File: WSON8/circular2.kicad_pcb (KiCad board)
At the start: 2 copper layers, 25 x 25 mm, 34 parts, among them J101 Conn_Coaxial, J102 Conn_01x03, U101 LT3042xMSE, U102 LT3093xMSE, U103 OPA859xDSG

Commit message: add ohwr-texts to wson8 files
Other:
- board text added: "Copyright Anders E E Wallin, 2020. This documentation describes Open Hardware and is licensed under the CERN OHL v. 1.2. You may redistribute and modify this documentation under the terms of the CERN OHL v.1.2. (http://ohwr.org/cernohl). This documentation is distributed WITHOUT ANY EXPRESS OR IMPLIED WARRANTY, INCLUDING OF MERCHANTABILITY, SATISFACTORY QUALITY AND FITNESS FOR A PARTICULAR PURPOS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"
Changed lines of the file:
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@@
   (general
     (thickness 1.6)
-    (drawings 23)
+    (drawings 28)
     (tracks 282)
     (zones 0)
@@
   )
   (page A4)
+  (title_block
+    (title "One Inch Photodetector - WSON8")
+    (date 2020-02)
+    (company "anders.e.e.wallin \"at\" gmail.com")
+  )
   (layers
     (0 F.Cu signal)
@@
     )
   )
+  (gr_line (start 210 40) (end 210 20) (layer Dwgs.User) (width 0.15))
+  (gr_line (start 280 40) (end 210 40) (layer Dwgs.User) (width 0.15))
+  (gr_line (start 280 20) (end 280 40) (layer Dwgs.User) (width 0.15))
+  (gr_line (start 210 20) (end 280 20) (layer Dwgs.User) (width 0.15))
+  (gr_text "Copyright Anders E E Wallin, 2020.\nThis documentation describes Open Hardware and is licensed under the\nCERN OHL v. 1.2.\nYou may redistribute and modify this documentation under the terms of the\nCERN OHL v.1.2. (http://ohwr.org/cernohl). This documentation is distributed\nWITHOUT ANY EXPRESS OR IMPLIED WARRANTY, INCLUDING OF\nMERCHANTABILITY, SATISFACTORY QUALITY AND FITNESS FOR A\nPARTICULAR PURPOSE. Please see the CERN OHL v.1.2 for applicable\nconditions\n" (at 216 30) (layer Dwgs.User)
+    (effects (font (size 1 1) (thickness 0.15)) (justify left))
+  )
   (gr_text - (at 160.25 101) (layer F.SilkS)

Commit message: save wson
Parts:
- C102, C110, C111: value C -> 4u7
- C104: value C -> 10n
- C108, C109: value C -> 100n
- R101, R107: value 49k9 -> 25k
- R103: value R -> 0R
- R106: value R -> 49R9
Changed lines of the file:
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@@
-(kicad_pcb (version 20171130) (host pcbnew 5.1.5-52549c5~84~ubuntu18.04.1)
+(kicad_pcb (version 20171130) (host pcbnew 5.1.5-52549c5~86~ubuntu18.04.1)
   (general
     (thickness 1.6)
@@
       (effects (font (size 0.5 0.5) (thickness 0.1)))
     )
-    (fp_text value 49k9 (at 0 1.43) (layer F.Fab)
+    (fp_text value 25k (at 0 1.43) (layer F.Fab)
       (effects (font (size 1 1) (thickness 0.15)))
     )
@@
       (effects (font (size 0.5 0.5) (thickness 0.1)))
     )
-    (fp_text value R (at 0 1.43 45) (layer F.Fab)
+    (fp_text value 49R9 (at 0 1.43 45) (layer F.Fab)
       (effects (font (size 1 1) (thickness 0.15)))
     )
@@
       (effects (font (size 0.5 0.5) (thickness 0.1)) (justify mirror))
     )
-    (fp_text value R (at 0 -1.43 90) (layer B.Fab)
+    (fp_text value 0R (at 0 -1.43 90) (layer B.Fab)
       (effects (font (size 1 1) (thickness 0.15)) (justify mirror))
     )
@@
       (effects (font (size 0.5 0.5) (thickness 0.1)) (justify mirror))
     )
-    (fp_text value 49k9 (at 0 -1.43 270) (layer B.Fab)
+    (fp_text value 25k (at 0 -1.43 270) (layer B.Fab)
       (effects (font (size 1 1) (thickness 0.15)) (justify mirror))
     )
@@
       (effects (font (size 0.5 0.5) (thickness 0.1)) (justify mirror))
     )
-    (fp_text value C (at 0 -1.43) (layer B.Fab)
+    (fp_text value 4u7 (at 0 -1.43) (layer B.Fab)
       (effects (font (size 1 1) (thickness 0.15)) (justify mirror))
     )
@@
       (effects (font (size 0.5 0.5) (thickness 0.1)))
     )
-    (fp_text value C (at 0 1.43) (layer F.Fab)
+    (fp_text value 4u7 (at 0 1.43) (layer F.Fab)
       (effects (font (size 1 1) (thickness 0.15)))
     )
@@
       (effects (font (size 0.5 0.5) (thickness 0.1)) (justify mirror))
     )
-    (fp_text value C (at 0 -1.43) (layer B.Fab)
+    (fp_text value 100n (at 0 -1.43) (layer B.Fab)
       (effects (font (size 1 1) (thickness 0.15)) (justify mirror))
     )
@@
       (effects (font (size 0.5 0.5) (thickness 0.1)))
     )
-    (fp_text value C (at 0 1.43) (layer F.Fab)
+    (fp_text value 100n (at 0 1.43) (layer F.Fab)
       (effects (font (size 1 1) (thickness 0.15)))
     )
@@
       (effects (font (size 0.5 0.5) (thickness 0.1)) (justify mirror))
     )
-    (fp_text value C (at 0 -1.43) (layer B.Fab)
+    (fp_text value 10n (at 0 -1.43) (layer B.Fab)
       (effects (font (size 1 1) (thickness 0.15)) (justify mirror))
     )
@@
       (effects (font (size 0.5 0.5) (thickness 0.1)) (justify mirror))
     )
-    (fp_text value C (at 0 -1.43) (layer B.Fab)
-      (effects (font (size 1 1) (thickness 0.15)) (justify mirror))
-    )
+    (fp_text value 4u7 (at 0 -1.43) (layer B.Fab)
+      (effects (font (size 1 1) (thickness 0.15)) (justify mirror))
+    )

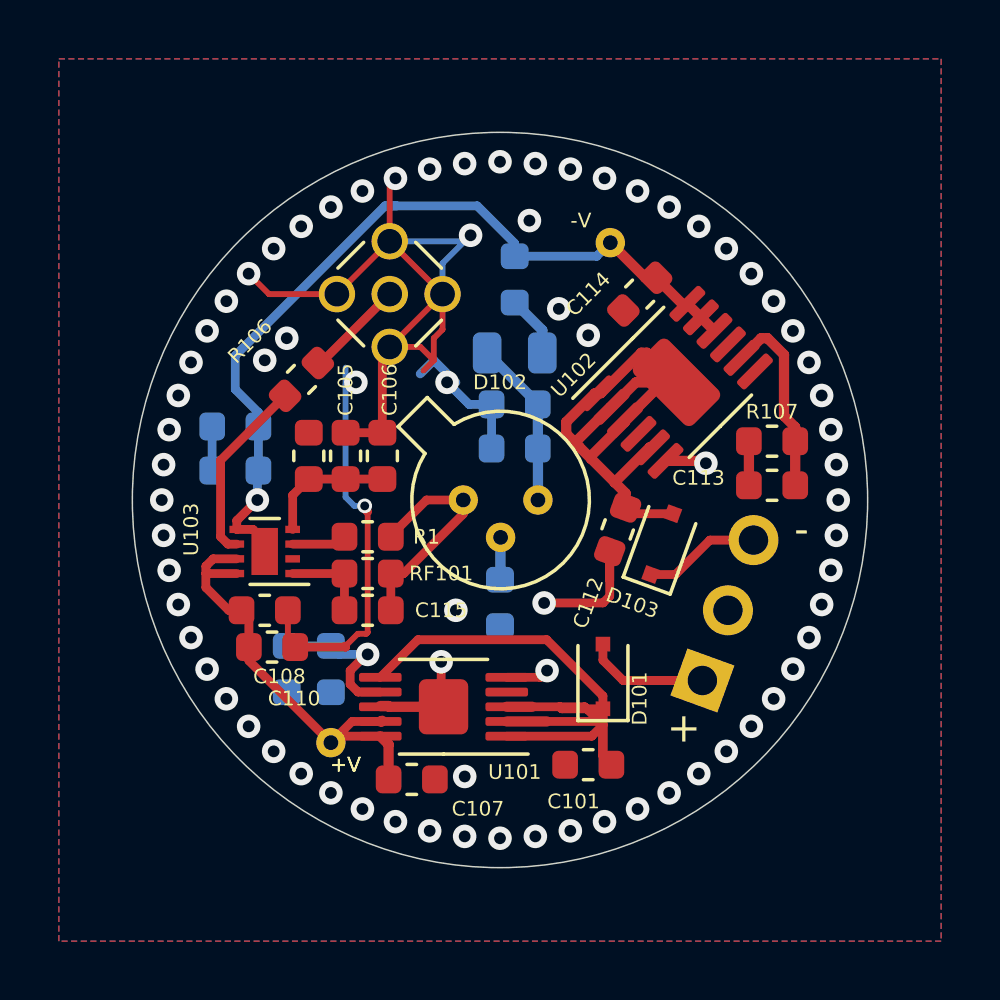
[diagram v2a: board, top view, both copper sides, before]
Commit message: add buffer to WSON8 design
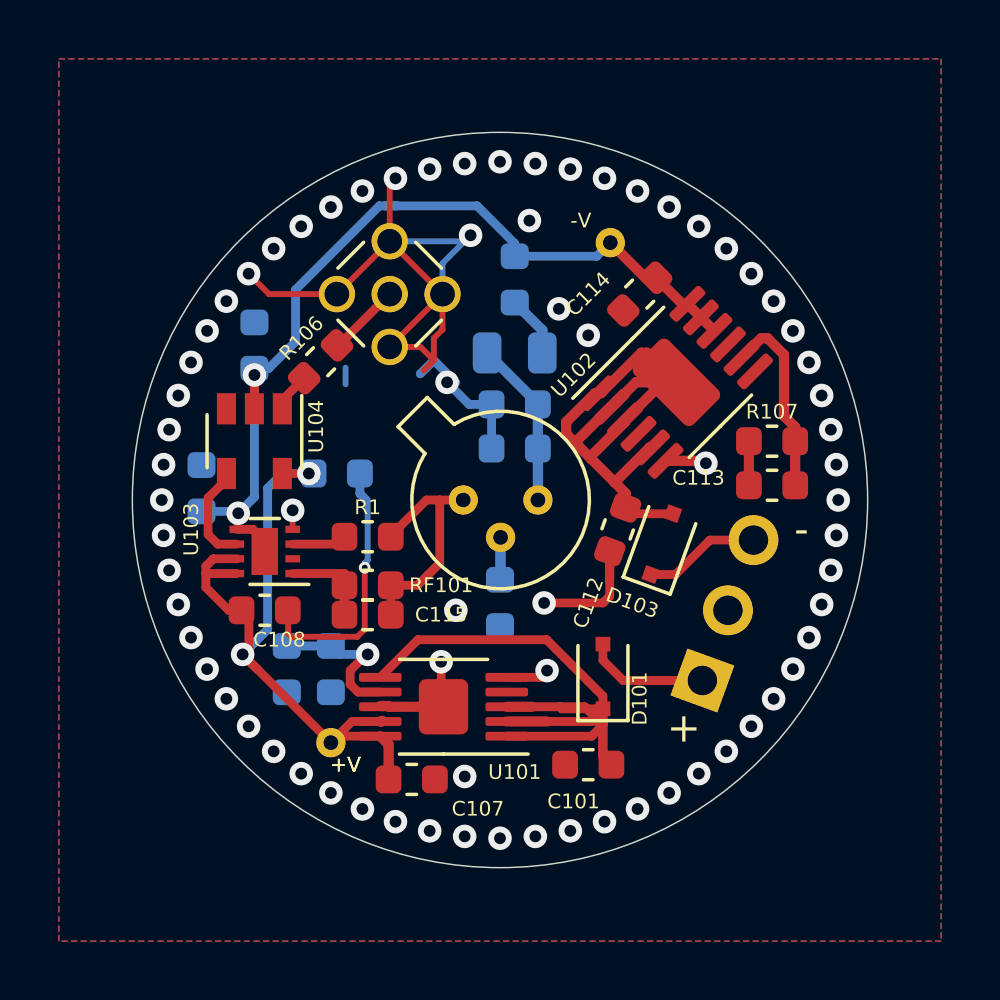
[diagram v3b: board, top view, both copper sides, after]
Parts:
- removed C110, C111: 4u7, Capacitor_SMD:C_0603_1608Metric
- removed R104: R, Resistor_SMD:R_0603_1608Metric
- added U104: BUF602xDBV, Package_TO_SOT_SMD:SOT-23-5, F.Cu at (141.7, 98.0)
- C105, C106: value C -> 100n; moved to B.Cu
- moved C106 5.74 mm to (141.7, 94.8)
- moved C109 1.30 mm to (139.8, 99.6), turned to 90 degrees
- moved R106 0.88 mm to (143.9, 95.3)
- moved C105 0.67 mm to (144.4, 99.1), turned to 180 degrees
- moved RF101 0.40 mm to (145.5, 102.9)
- moved C115 0.15 mm to (145.5, 103.9)
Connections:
- C105 pad 1: /IN+ -> GND
- C105 pad 2: GND -> /+V
- C106 pad 1: /IN+ -> /-V
- U103 pad 4: /IN+ -> GND
- U103 pad 6: /VOUT -> /VTIA
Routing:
- net GND: track 62.1 -> 51.7 mm, vias 75 -> 73
- net /+V: track 15.6 -> 24.8 mm, vias 0 -> 2
- net /VOUT: track 6.36 -> 1.35 mm
- net /IN+: track 4.44 -> 0.00 mm
- net /VTIA: track 0.00 -> 3.44 mm
- net /-V: track 29.2 -> 31.4 mm, vias 1 -> 2
- net Net-(J101-Pad1): track 3.41 -> 2.52 mm
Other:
- board text added: "1" Photodetector AW2020-05-12"
- board text removed: "1" Photodetector AW2020-01-31"

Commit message: flip connector to bottom side
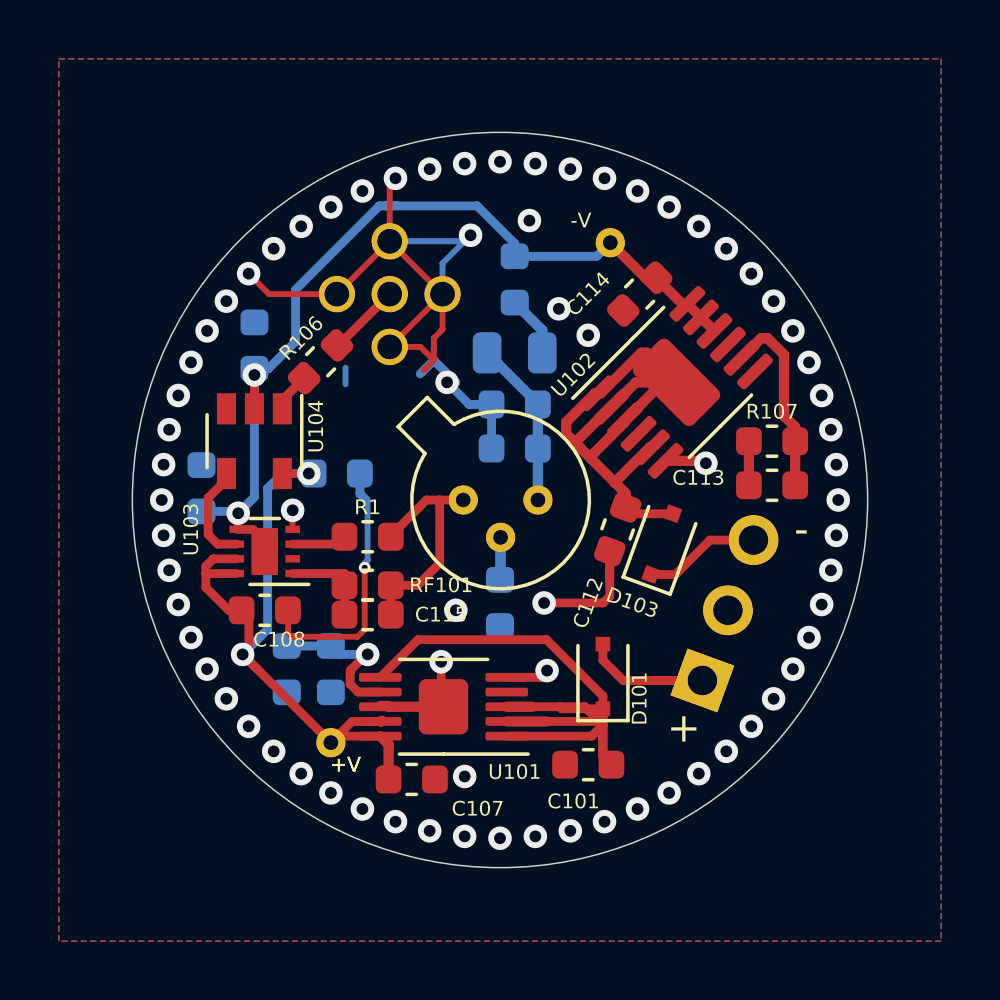
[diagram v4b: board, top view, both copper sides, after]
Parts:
- J101: moved to B.Cu
- turned J101 to 315 degrees
